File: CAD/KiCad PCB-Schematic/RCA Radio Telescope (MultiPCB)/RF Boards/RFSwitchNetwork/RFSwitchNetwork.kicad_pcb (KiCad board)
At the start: 2 copper layers, 0 parts

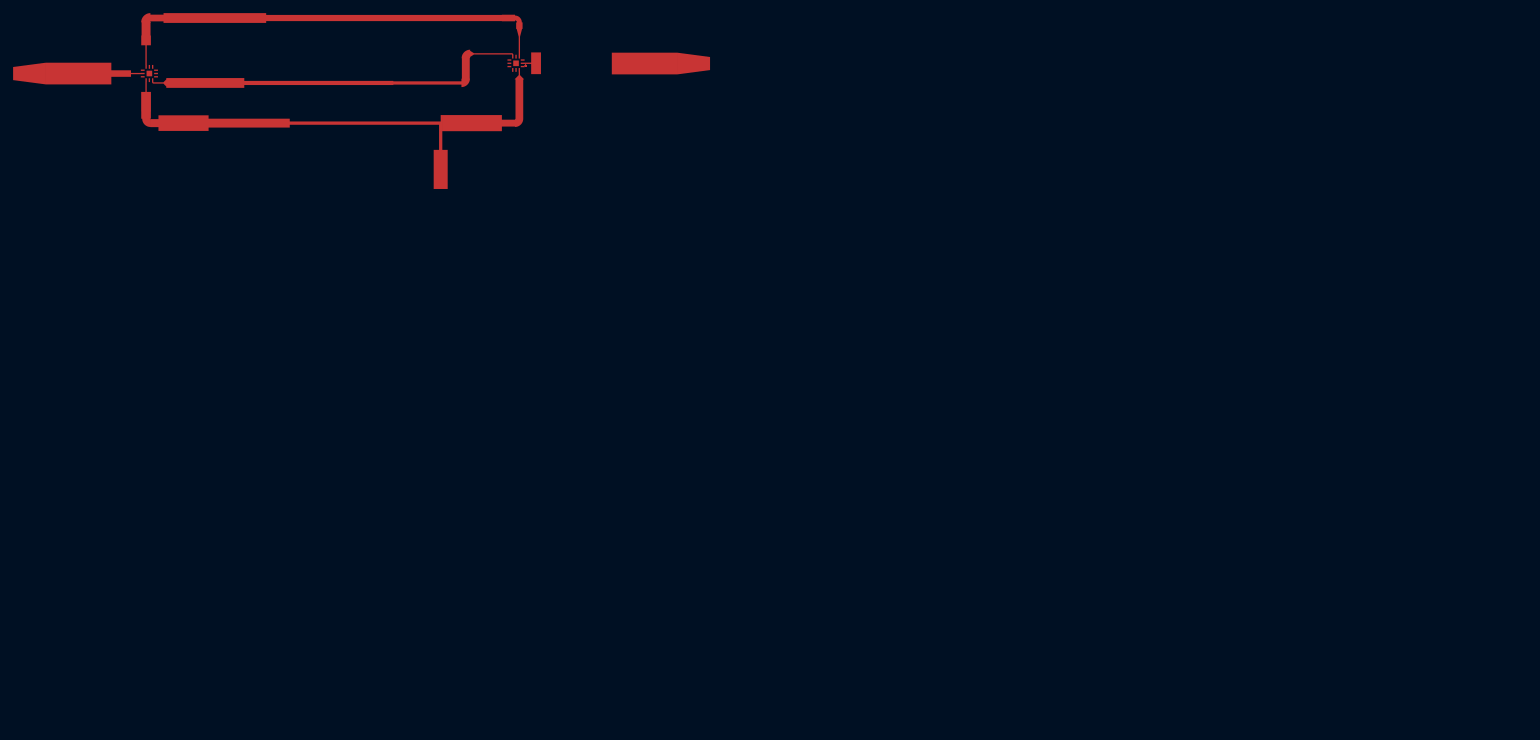
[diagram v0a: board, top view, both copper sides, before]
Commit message: Added 4 RF Board Designs into KiCAD project
- Added Matched SMD Filter Board, Matched Distributive Filter Board, RF Switch Filter Board, and kept original SMD Filter Board
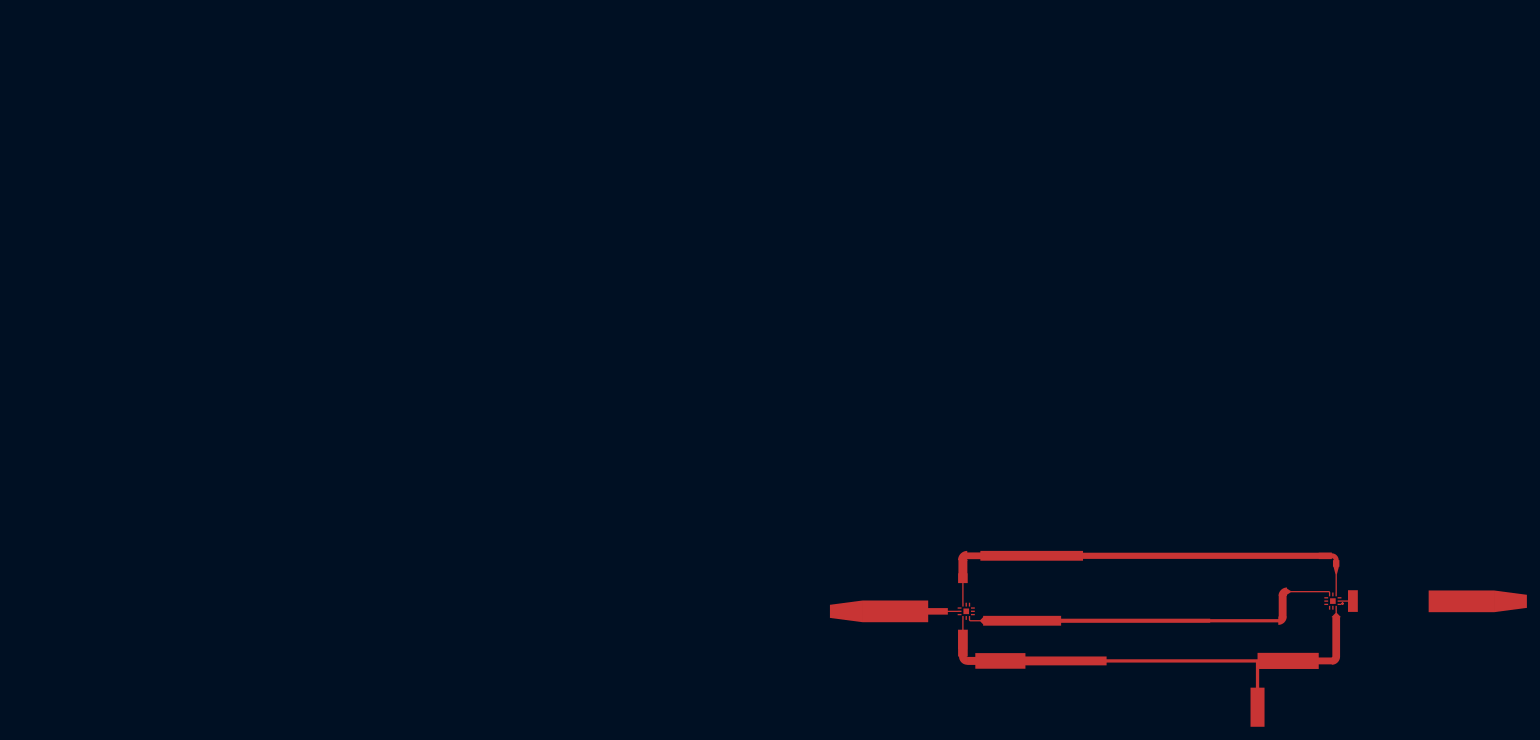
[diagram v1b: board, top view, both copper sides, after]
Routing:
- net 0: track 1.04 -> 0.00 mm
- net (no net): track 0.00 -> 1.04 mm
